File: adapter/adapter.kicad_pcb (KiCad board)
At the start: 2 copper layers, 93.5 x 50.9 mm, 64 parts, among them J1 Serial, J10 Ribbon, J11 Ribbon, J12 Ribbon, J13 serial, J14 serial, J2 Serial, J3 battery charge, J4 RGB, J5 RGB, J6 battery charge, J7 trackball, J8 trackball, J9 Ribbon, SW1 SW_SPST, SW2 SW_SPST, SW3 SW_SPDT, SW4 SW_SPDT, U1 eliteC, U2 eliteC

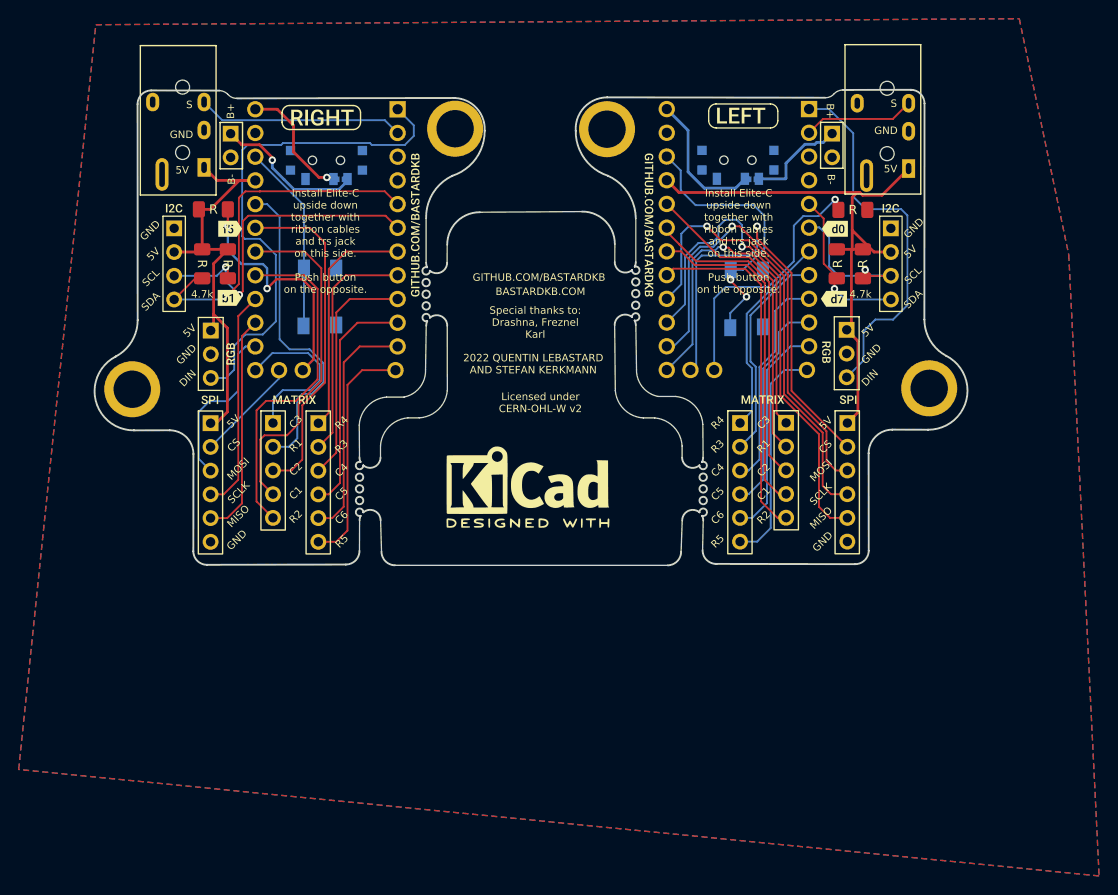
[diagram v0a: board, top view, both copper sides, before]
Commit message: Remove all of the components except matrix pins and add nice!nano schematic from github
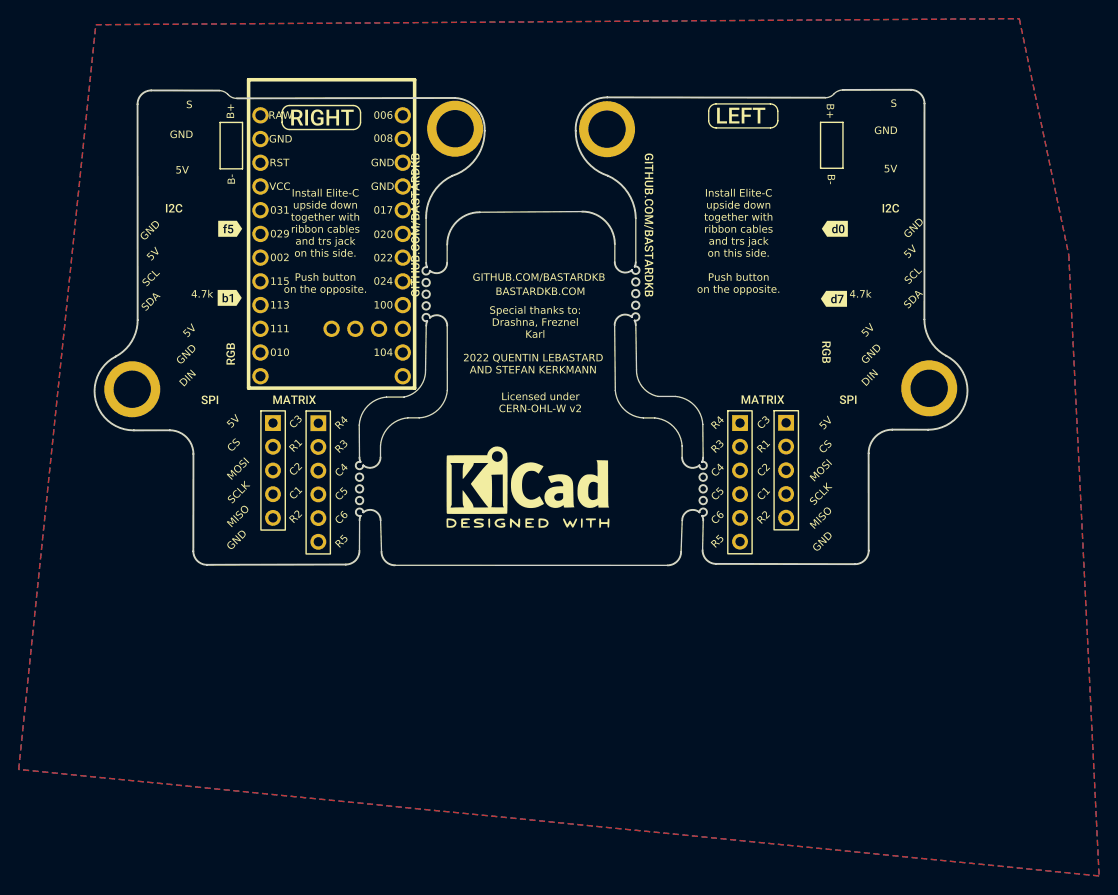
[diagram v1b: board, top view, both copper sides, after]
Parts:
- removed J1, J2: Serial, Library:Jack_3.5mm_PJ320E_Horizontal
- removed J13, J14: serial, Library:PinHeader_1x04_P2.54mm_Vertical
- removed J3, J6: battery charge, Library:PinHeader_1x02_P2.54mm_Vertical
- removed J4, J5: RGB, Library:header1x03
- removed J7, J8: trackball, Library:6_PinHeader
- removed JP1, JP2: Jumper_2_Open, Library:power_switch_jumper
- removed R1, R3, R5, R6: 5.1k, Library:R_1206_handsolder
- removed R2, R4: 4.7k, Library:R_1206_handsolder
- removed SW1, SW2: SW_SPST, Library:PushSwitch
- removed SW3, SW4: SW_SPDT, Library:SW_SPDT+H-MSK12C01_hor(7pin_SMD)
- removed U2: eliteC, Library:Elite-C
- U1: value eliteC -> nice_nano; footprint Library:Elite-C -> Library:nice_nano
- moved U1 0.85 mm to (134.1, 83.8)
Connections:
- U1 pad 1: rgb_r -> unconnected-(U1-TX0/P0.06-Pad1)
- U1 pad 10: col5_l -> unconnected-(U1-P0.11-Pad10)
- U1 pad 11: col6_l -> unconnected-(U1-P1.04-Pad11)
- U1 pad 12: row5_l -> unconnected-(U1-P1.06-Pad12)
- U1 pad 13: col3_l -> unconnected-(U1-NFC1/P0.09-Pad13)
- U1 pad 14: mosi_l -> unconnected-(U1-NFC2/P0.10-Pad14)
- U1 pad 15: miso_l -> unconnected-(U1-P1.11-Pad15)
- U1 pad 16: sc_l -> unconnected-(U1-P1.13-Pad16)
- U1 pad 17: row2_l -> unconnected-(U1-P1.15-Pad17)
- U1 pad 18: col1_l -> unconnected-(U1-AIN0/P0.02-Pad18)
- U1 pad 19: col2_l -> unconnected-(U1-AIN5/P0.29-Pad19)
- U1 pad 2: serial_l -> unconnected-(U1-RX1/P0.08-Pad2)
- U1 pad 20: row1_l -> unconnected-(U1-AIN7/P0.31-Pad20)
- U1 pad 21: +5V -> unconnected-(U1-VCC-Pad21)
- U1 pad 22: Rst -> unconnected-(U1-RST-Pad22)
- U1 pad 23: GND -> unconnected-(U1-GND-Pad23)
- U1 pad 24: bat_l -> unconnected-(U1-BATIN/P0.04-Pad24)
- U1 pad 3: GND -> unconnected-(U1-GND-Pad3)
- U1 pad 4: GND -> unconnected-(U1-GND-Pad4)
- U1 pad 5: sda_l -> unconnected-(U1-P0.17-Pad5)
- U1 pad 6: scl_l -> unconnected-(U1-P0.20-Pad6)
- U1 pad 7: row4_l -> unconnected-(U1-P0.22-Pad7)
- U1 pad 8: row3_l -> unconnected-(U1-P0.24-Pad8)
- U1 pad 9: col4_l -> unconnected-(U1-P1.00-Pad9)
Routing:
- net +5V: track 108.3 -> 0.00 mm
- net rgb_r: track 54.5 -> 0.00 mm
- net miso_r: track 54.1 -> 0.00 mm, vias 1 -> 0
- net mosi_r: track 49.5 -> 0.00 mm, vias 1 -> 0
- net ss_r: track 49.0 -> 0.00 mm, vias 1 -> 0
- net sc_r: track 48.4 -> 0.00 mm, vias 1 -> 0
- net rgb_l: track 40.4 -> 0.00 mm
- net col3_r: track 39.8 -> 0.00 mm, vias 1 -> 0
- net sda_l: track 38.7 -> 0.00 mm, vias 1 -> 0
- net row2_r: track 37.7 -> 0.00 mm
- net row2_l: track 37.1 -> 0.00 mm
- net col1_l: track 36.7 -> 0.00 mm
- net scl_l: track 36.2 -> 0.00 mm, vias 2 -> 0
- net col2_l: track 36.0 -> 0.00 mm
- net col1_r: track 35.9 -> 0.00 mm
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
